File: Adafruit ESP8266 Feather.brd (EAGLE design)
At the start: 50.8 x 22.9 mm, 40 parts, among them IC1 CP2104, Q1 mmbt2222, Q2 mmbt2222, SW2 KMR2, U2 SPX3819, U3 MCP73831T-2ACI/OT, X1 JSTPH, X2 ESP-12, X4 20329

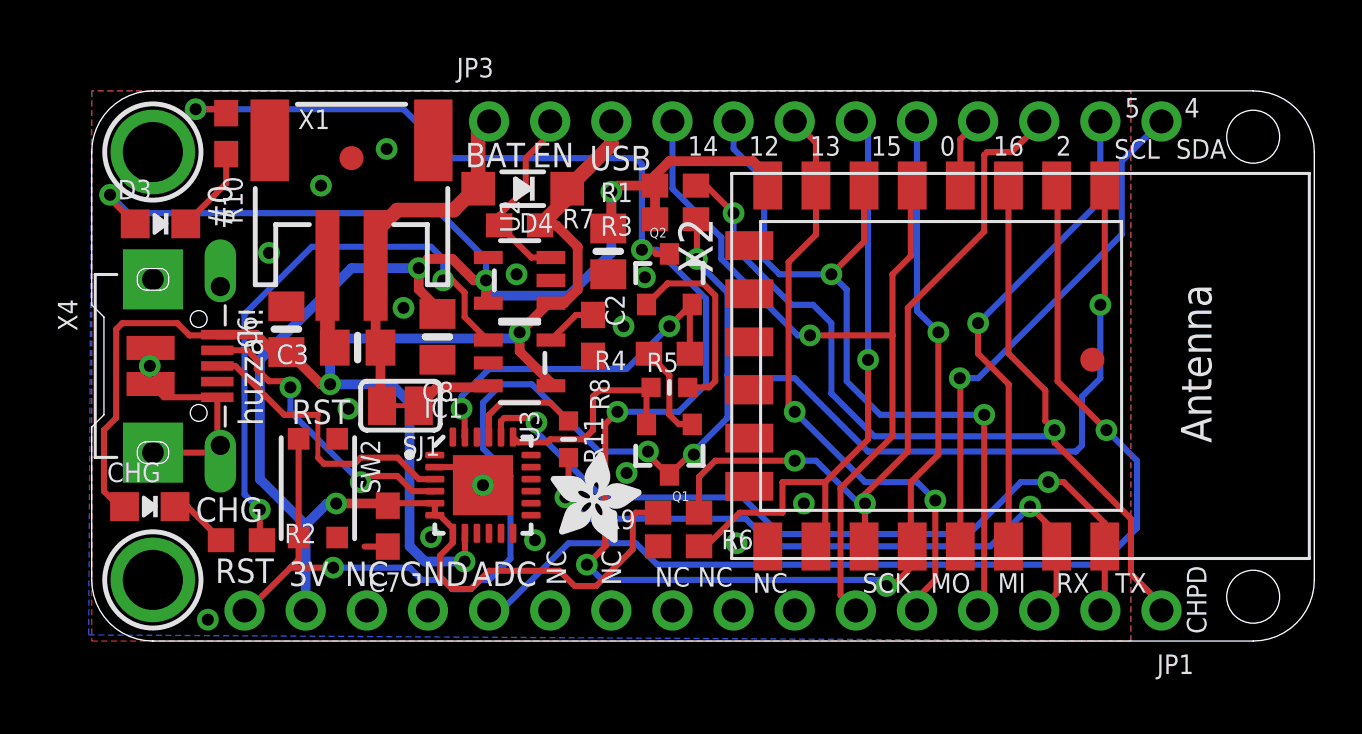
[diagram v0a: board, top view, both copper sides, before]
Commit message: added low cost version
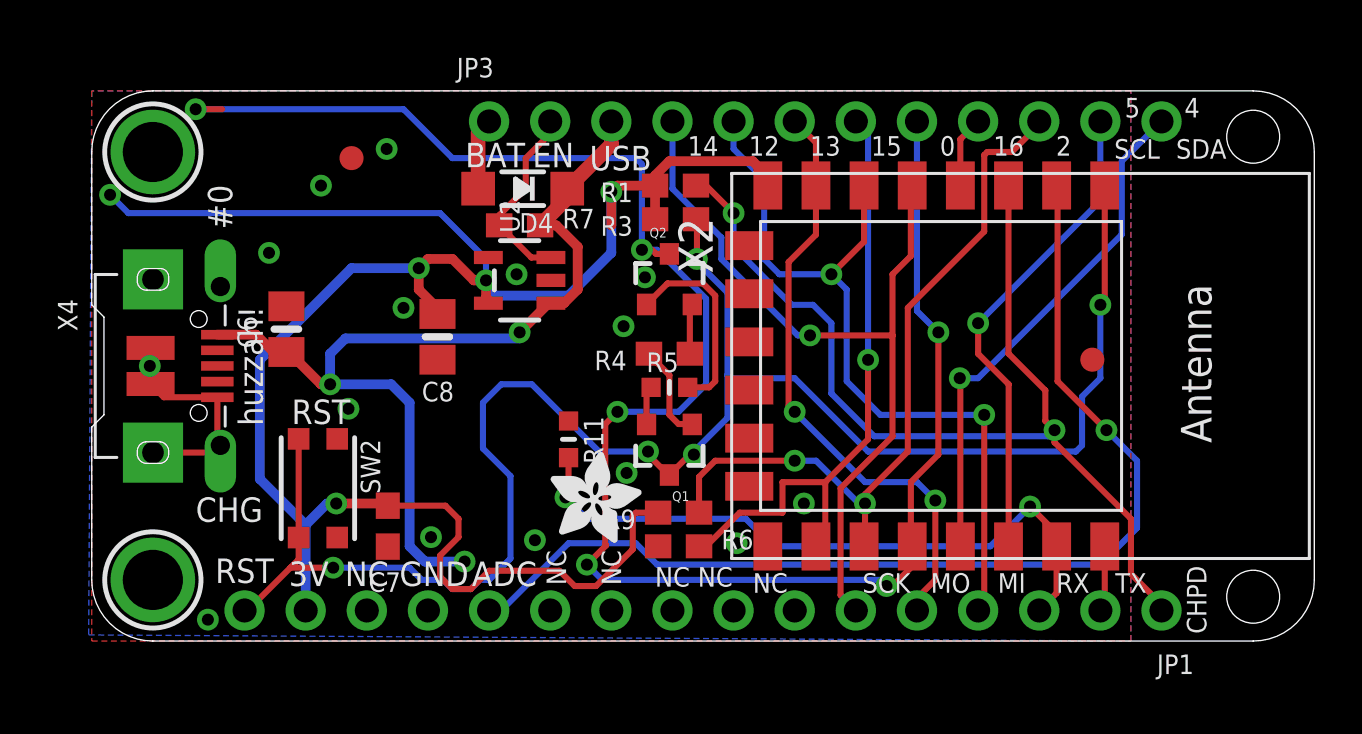
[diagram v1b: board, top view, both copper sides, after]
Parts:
- removed C2: 10uF, microbuilder:0805-NO
- removed C3: 10µF, microbuilder:0805-NO
- removed CHG: ORANGE, microbuilder:CHIPLED_0805_NOOUTLINE
- removed D3: RED, microbuilder:CHIPLED_0805_NOOUTLINE
- removed IC1: CP2104, microbuilder:QFN24_4MM_SMSC
- removed R10, R2: 1K, microbuilder:0603-NO
- removed R8: 10K\, microbuilder:0603-NO
- removed SJ1: (no value), microbuilder:SOLDERJUMPER_CLOSEDWIRE
- removed U3: MCP73831T-2ACI/OT, microbuilder:SOT23-5
- removed X1: JSTPH, microbuilder:JSTPH2
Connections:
- removed net N$1: CHG.C, R2.1
- removed net N$2: IC1.3, X4.D+
- removed net N$3: R2.2, U3.1
- removed net N$4: R8.1, U3.5
- removed net N$5: D3.C, R10.2
- removed net N$6: IC1.4, X4.D-
- removed net N$7: SJ1.1, U3.3
- net 3.3V: no longer C2.1, D3.A, IC1.5, IC1.6, IC1.7
- net DTR: no longer IC1.23
- net GND: no longer C2.2, C3.2, IC1.2, IC1.THERM, R8.2, U3.2, X1.1
- net GPIO0: no longer R10.1
- net RTS: no longer IC1.19
- net TXD: no longer IC1.20
- net USB_RX: no longer IC1.21
- net VBAT: no longer C3.1, SJ1.2, X1.2
- net VBUS: no longer CHG.A, IC1.8, U3.4
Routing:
- net TXD: track 33.3 -> 2.74 mm, vias 2 -> 0
- net N$3: track 23.7 -> 0.00 mm, vias 2 -> 0
- net VBUS: track 56.3 -> 39.8 mm
- net DTR: track 15.1 -> 2.15 mm, vias 2 -> 0
- net VBAT: track 15.5 -> 2.98 mm
- net N$6: track 12.5 -> 0.00 mm, vias 2 -> 0
- net N$2: track 12.2 -> 0.00 mm
- net RTS: track 9.03 -> 1.62 mm
- net GND: track 16.7 -> 9.63 mm, vias 16 -> 15
- net USB_RX: track 4.75 -> 0.00 mm
- net N$5: track 3.59 -> 0.00 mm
- net N$7: track 3.23 -> 0.00 mm
- net N$1: track 2.49 -> 0.00 mm
- net N$4: track 2.18 -> 0.00 mm
- net 3.3V: track 86.4 -> 85.3 mm

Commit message: through hole parts
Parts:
- removed Q1, Q2: mmbt2222, SparkFun:SOT23-3
- removed R1, R4, R7, R9: 10K, microbuilder:0603-NO
- removed R11: 1K, microbuilder:_0603MP
- removed R5: 10K, microbuilder:_0603MP
- removed R6: 4.7K, microbuilder:0603-NO
- removed SW2: KMR2, microbuilder:BTN_KMR2_4.6X2.8
- removed U$34, U$35: FIDUCIAL"", microbuilder:FIDUCIAL_1MM
- removed U2: SPX3819, microbuilder:SOT23-5
- removed X4: 20329, microbuilder:4UCONN_20329_V2
- added IC2: LD117AV33, v-reg:TO220L1
- added SW1: (no value), adafruit:TACT_PANA-EVQ
- C6, C8: device microbuilder:0805-NO -> rcl:C025-024X044
- C7: device microbuilder:0603-NO -> rcl:C025-024X044
- D4: device microbuilder:SOD-123 -> adafruit:DO41-7
- R3: device microbuilder:0603-NO -> rcl:0204/5
- moved U$15 17.5 mm to (1.59, 4.06)
- moved C6 13.4 mm to (21.4, 11.4)
- moved C7 8.91 mm to (21.2, 5.41)
- moved C8 8.58 mm to (21.2, 17.8), turned to 90 degrees
- moved D4 7.18 mm to (17.8, 11.6), turned to 90 degrees
- moved R3 6.22 mm to (24.2, 11.3), turned to 90 degrees
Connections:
- removed net DTR: Q2.2, R4.1
- removed net N$12: Q1.1, R4.2
- removed net N$13: Q2.1, R5.2
- removed net RTS: Q1.2, R5.1
- removed net USB_RX: R11.1
- net 3.3V: now also IC2.2; no longer R1.2, R9.2, U2.5
- net CH_PD: no longer R1.1
- net EN: no longer R7.1, U2.3
- net GND: now also IC2.1, SW1.P$2; no longer R6.1, SW2.A, SW2.A', U2.2, X4.BASE@1, X4.BASE@2, X4.GND, X4.SPRT@1, X4.SPRT@2, X4.SPRT@3, X4.SPRT@4
- net GPIO0: no longer Q2.3
- net GPIO15: no longer R6.2
- net GPIO2: no longer R9.1
- net RESET: now also SW1.P$1; no longer Q1.3, SW2.B, SW2.B'
- net RXD: no longer R11.2
- net VBUS: now also IC2.3; no longer R7.2, U2.1, X4.VBUS
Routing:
- net GPIO0: track 77.4 -> 20.1 mm, vias 6 -> 1
- net 3.3V: track 85.3 -> 49.2 mm, vias 5 -> 0
- net RXD: track 27.6 -> 2.96 mm, vias 2 -> 0
- net CH_PD: track 42.4 -> 20.3 mm, vias 2 -> 0
- net RESET: track 74.4 -> 60.5 mm, vias 5 -> 3
- net ADC: track 44.7 -> 32.2 mm
- net N$13: track 8.23 -> 0.00 mm
- net GPIO2: track 30.7 -> 22.6 mm, vias 2 -> 1
- net EN: track 7.90 -> 0.00 mm
- net GPIO14/SCK: track 34.1 -> 40.5 mm
- net GPIO15: track 25.9 -> 20.9 mm
- net N$12: track 4.01 -> 0.00 mm
- net VBAT: track 2.98 -> 6.52 mm
- net GPIO12/MISO: track 32.8 -> 29.3 mm
- net GPIO13/MOSI: track 25.3 -> 22.3 mm, vias 2 -> 1
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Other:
- board text removed: "CHG"
- board text removed: "huzzah!"
